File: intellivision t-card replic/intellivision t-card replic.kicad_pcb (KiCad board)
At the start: 2 copper layers, 143 x 165.9 mm, 77 parts, among them J1 2x22 card edge connector, SW1 SW_DIP_x08, SW2 SW_DIP_x08, SW3 SW_DIP_x08, SW4 SW_DIP_x08, U1 74LS374, U10 74LS00, U11 74LS85, U12 74LS51, U13 74LS00, U14 74LS85, U15 74LS51, U16 74LS00, U17 74LS85, U18 2732, U19 2732, U2 74LS374, U20 2732, U21 2732, U22 2732, U23 2732, U24 2732, U25 2732, U3 74LS42, U4 74LS04, U5 74LS08, U6 74LS51, U7 74LS00, U8 74LS85, U9 74LS51

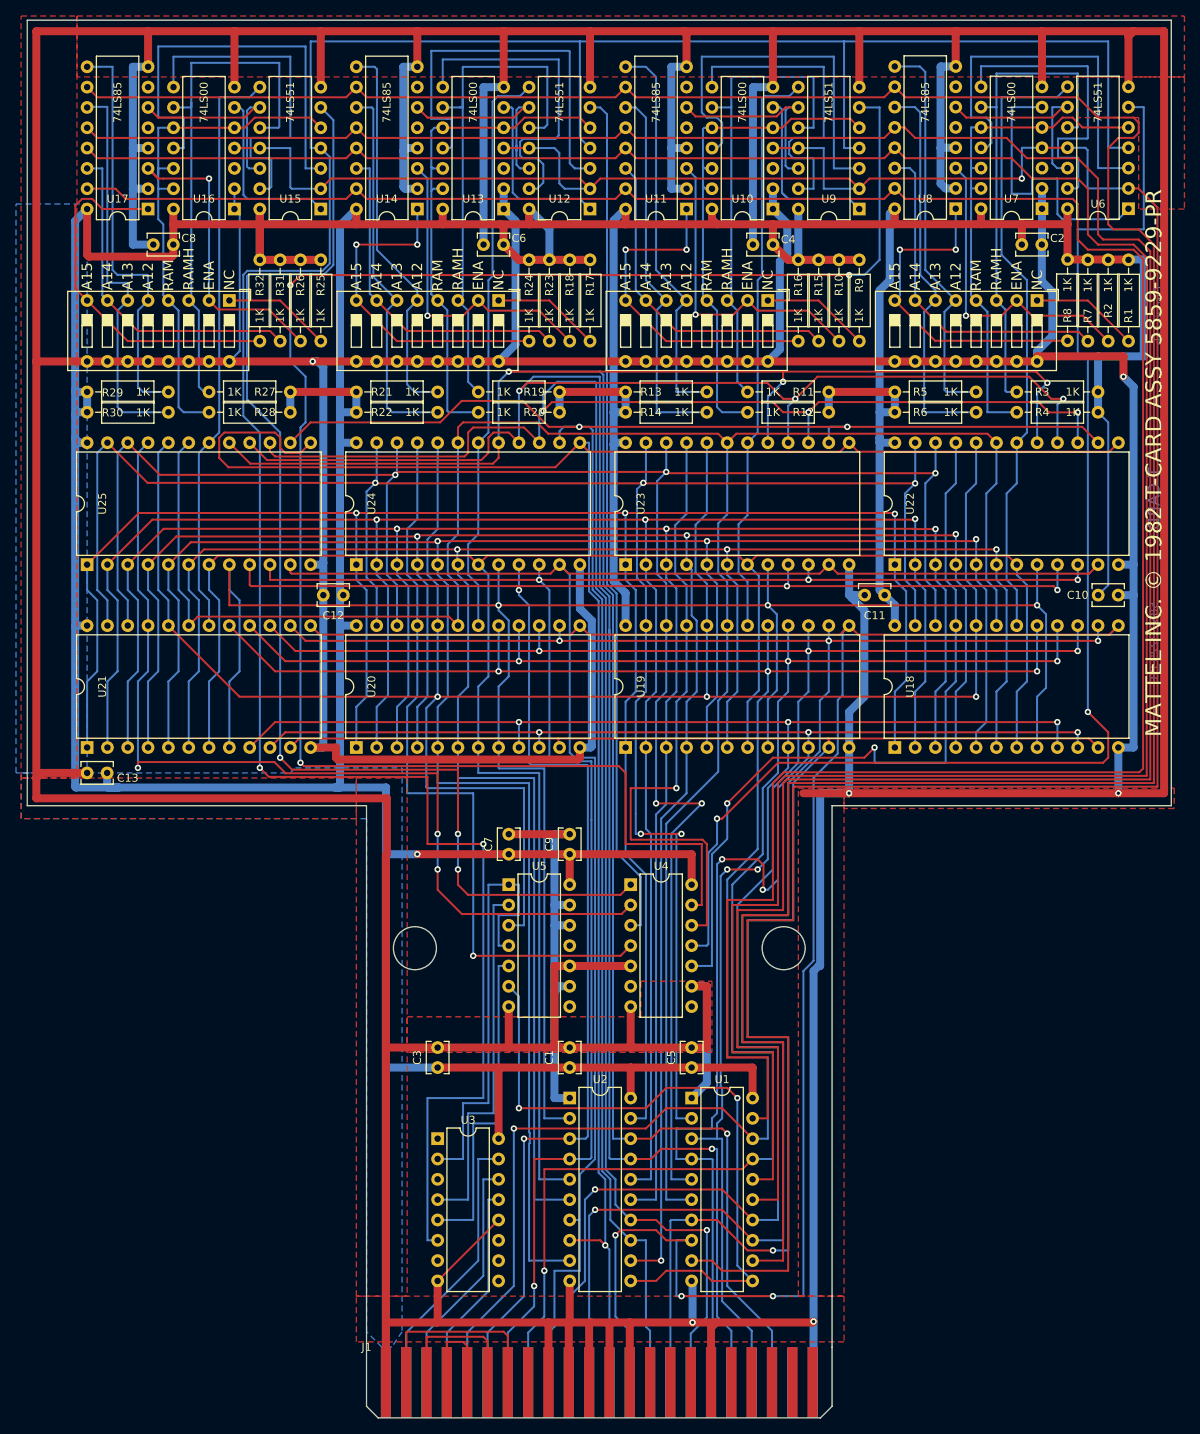
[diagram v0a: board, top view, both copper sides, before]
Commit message: added gitignore
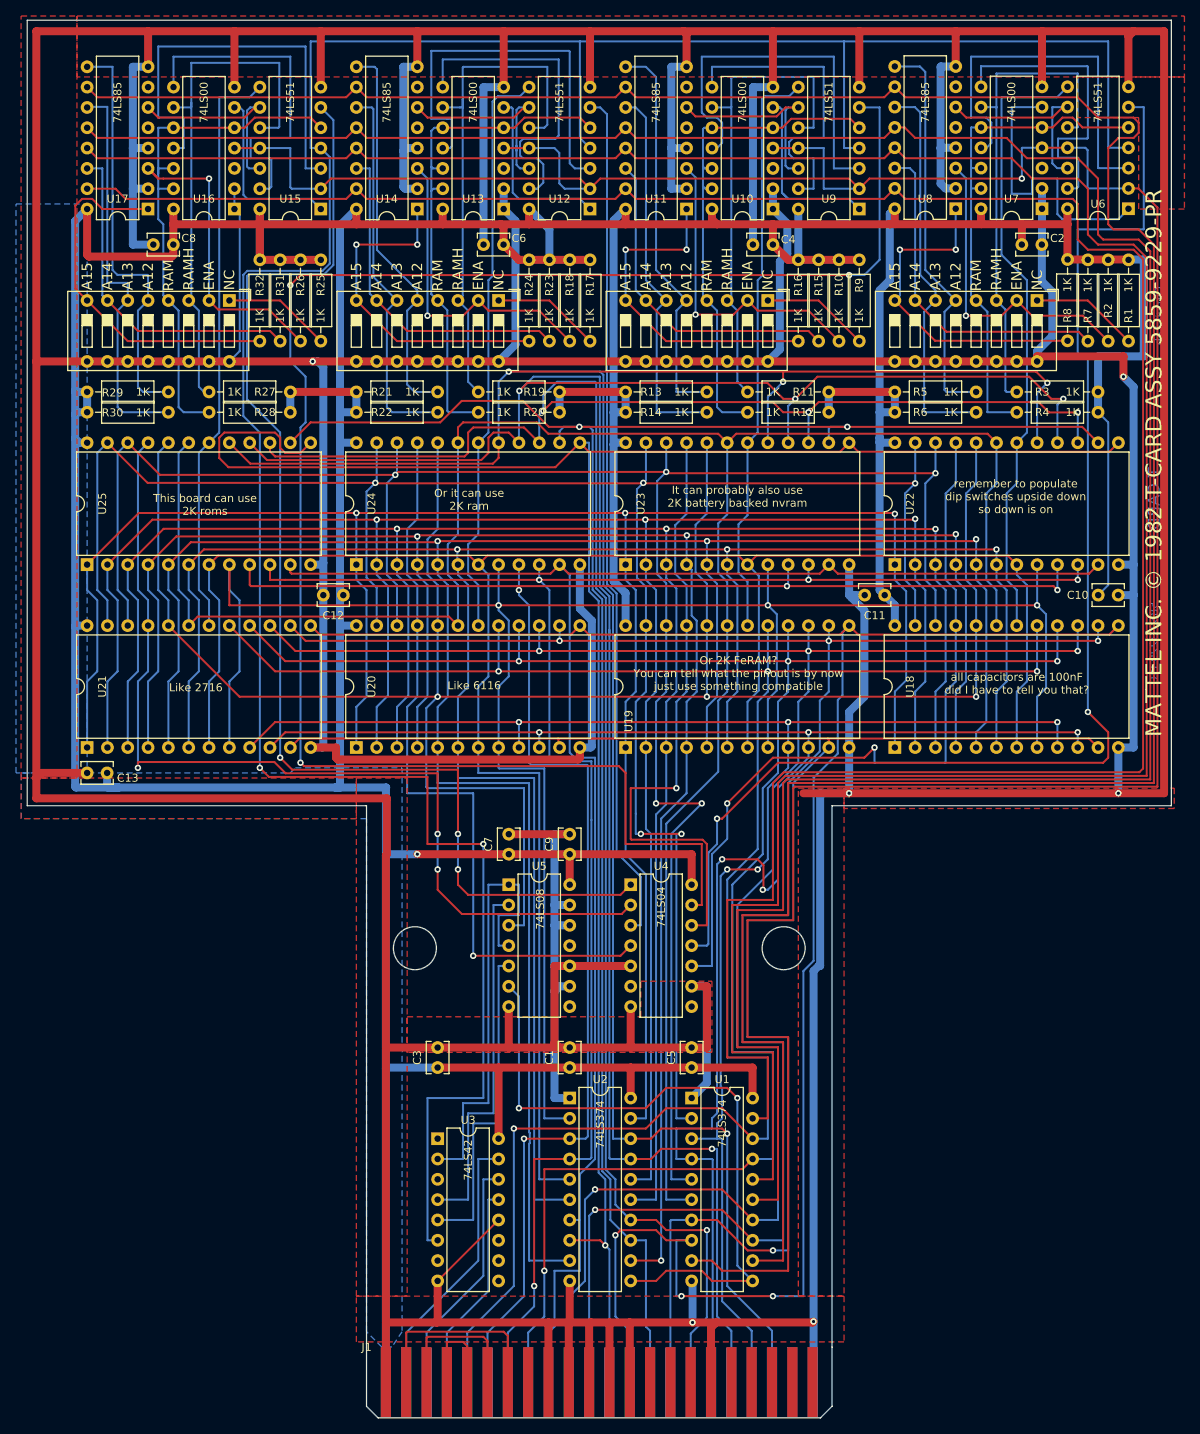
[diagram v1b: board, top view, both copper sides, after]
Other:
- board text added: "It can probably also use 2K battery backed nvram"
- board text added: "Like 2716"
- board text added: "Like 6116"
- board text added: "Or 2K FeRAM? You can tell what the pinout is by now just use something compatible"
- board text added: "Or it can use 2K ram"
- board text added: "This board can use 2K roms"
- board text added: "all capacitors are 100nF did I have to tell you that?"
- board text added: "remember to populate dip switches upside down so down is on"
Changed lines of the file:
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@@
       (effects (font (size 1 1) (thickness 0.15)))
     )
-    (fp_text value "74LS04" (at 3.81 17.57) (layer "F.Fab")
+    (fp_text value "74LS04" (at 3.81 2.794 90) (layer "F.SilkS")
       (effects (font (size 1 1) (thickness 0.15)))
     )
@@
       (effects (font (size 1 1) (thickness 0.15)))
     )
-    (fp_text value "74LS42" (at 3.81 20.11) (layer "F.Fab")
+    (fp_text value "74LS42" (at 3.81 2.667 90) (layer "F.SilkS")
       (effects (font (size 1 1) (thickness 0.15)))
     )
@@
       (effects (font (size 1 1) (thickness 0.15)))
     )
-    (fp_text value "74LS374" (at 3.81 25.19) (layer "F.Fab")
+    (fp_text value "74LS374" (at 3.81 3.302 90) (layer "F.SilkS")
       (effects (font (size 1 1) (thickness 0.15)))
     )
@@
       (effects (font (size 1 1) (thickness 0.15)))
     )
-    (fp_text value "74LS374" (at 3.81 25.19) (layer "F.Fab")
+    (fp_text value "74LS374" (at 3.81 3.175 90) (layer "F.SilkS")
       (effects (font (size 1 1) (thickness 0.15)))
     )
@@
     (property "Sheetname" "intellivision roms")
     (attr through_hole)
-    (fp_text reference "U19" (at 7.62 1.905 90) (layer "F.SilkS")
+    (fp_text reference "U19" (at 3.302 0.381 90) (layer "F.SilkS")
       (effects (font (size 1 1) (thickness 0.15)))
     )
@@
       (effects (font (size 1 1) (thickness 0.15)))
     )
-    (fp_text value "74LS08" (at 3.81 17.57) (layer "F.Fab")
+    (fp_text value "74LS08" (at 3.937 3.048 90) (layer "F.SilkS")
       (effects (font (size 1 1) (thickness 0.15)))
     )
@@
     (effects (font (size 1 1) (thickness 0.15)) (justify mirror))
   )
+  (gr_text "Like 6116" (at 102.362 100.838) (layer "F.SilkS")
+    (effects (font (size 1 1) (thickness 0.15)))
+  )
   (gr_text "A12" (at 128.905 51.435 90) (layer "F.SilkS")
     (effects (font (size 1.3 1.3) (thickness 0.2)) (justify left))
@@
     (effects (font (size 1.3 1.3) (thickness 0.2)) (justify left))
   )
+  (gr_text "Like 2716" (at 67.564 101.092) (layer "F.SilkS")
+    (effects (font (size 1 1) (thickness 0.15)))
+  )
   (gr_text "NC" (at 105.41 51.435 90) (layer "F.SilkS")
     (effects (font (size 1.3 1.3) (thickness 0.2)) (justify left))
@@
     (effects (font (size 1.3 1.3) (thickness 0.2)) (justify left))
   )
+  (gr_text "Or it can use \n2K ram" (at 101.727 77.597) (layer "F.SilkS")
+    (effects (font (size 1 1) (thickness 0.15)))
+  )
   (gr_text "RAMH" (at 66.675 51.435 90) (layer "F.SilkS")
     (effects (font (size 1.3 1.3) (thickness 0.2)) (justify left))
   )
+  (gr_text "remember to populate \ndip switches upside down\nso down is on" (at 170.053 77.216) (layer "F.SilkS")
+    (effects (font (size 1 1) (thickness 0.15)))
+  )
+  (gr_text "all capacitors are 100nF\ndid I have to tell you that?" (at 170.18 100.584) (layer "F.SilkS")
+    (effects (font (size 1 1) (thickness 0.15)))
+  )
   (gr_text "A12" (at 162.56 51.435 90) (layer "F.SilkS")
     (effects (font (size 1.3 1.3) (thickness 0.2)) (justify left))
@@
     (effects (font (size 1.3 1.3) (thickness 0.2)) (justify left))
   )
+  (gr_text "Or 2K FeRAM? \nYou can tell what the pinout is by now\njust use something compatible" (at 135.382 99.314) (layer "F.SilkS")
+    (effects (font (size 1 1) (thickness 0.15)))
+  )
   (gr_text "ENA" (at 102.87 51.435 90) (layer "F.SilkS")
     (effects (font (size 1.3 1.3) (thickness 0.2)) (justify left))
@@
     (effects (font (size 1.3 1.3) (thickness 0.2)) (justify left))
   )
+  (gr_text "It can probably also use \n2K battery backed nvram" (at 135.255 77.216) (layer "F.SilkS")
+    (effects (font (size 1 1) (thickness 0.15)))
+  )
   (gr_text "A13" (at 126.365 51.435 90) (layer "F.SilkS")
     (effects (font (size 1.3 1.3) (thickness 0.2)) (justify left))
@@
     (effects (font (size 1.3 1.3) (thickness 0.2)) (justify left))
   )
+  (gr_text "This board can use\n2K roms" (at 68.707 78.232) (layer "F.SilkS")
+    (effects (font (size 1 1) (thickness 0.15)))
+  )
   (gr_text "RAM" (at 165.1 51.565 90) (layer "F.SilkS")

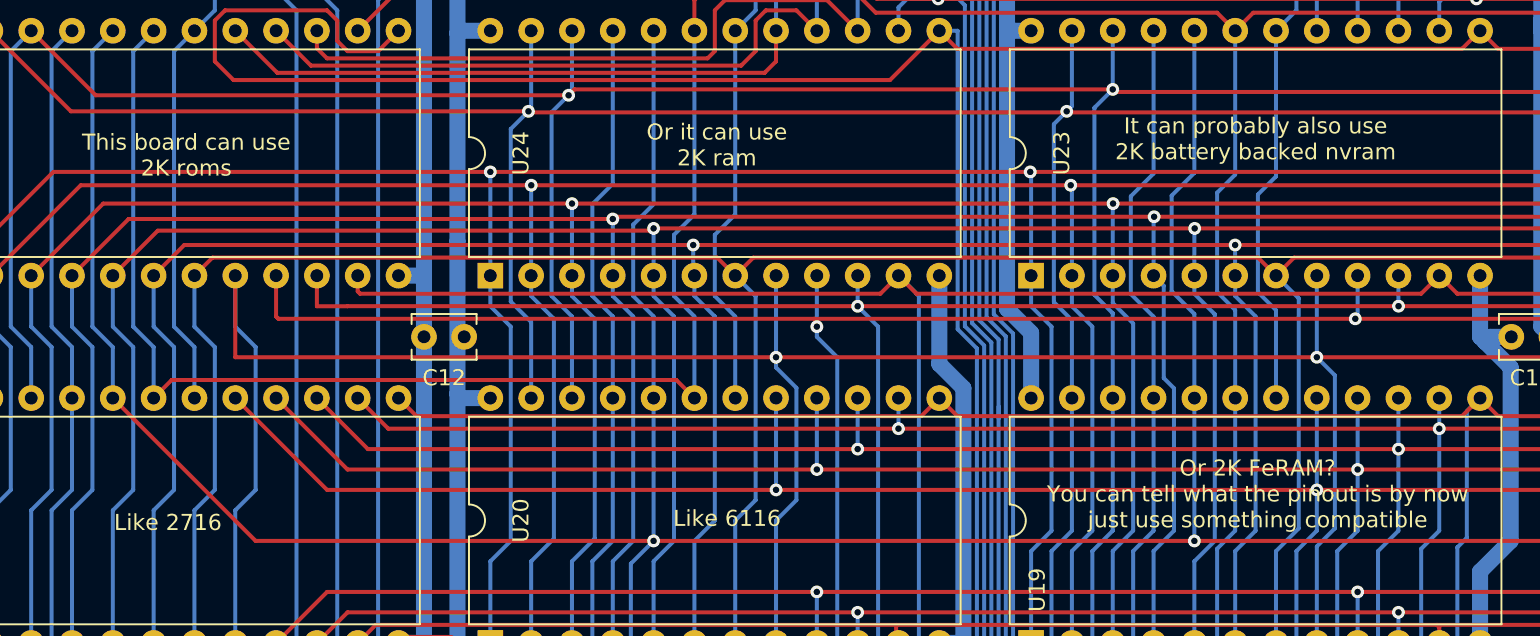
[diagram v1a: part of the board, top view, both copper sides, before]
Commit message: fixed silk about 2k/4k roms
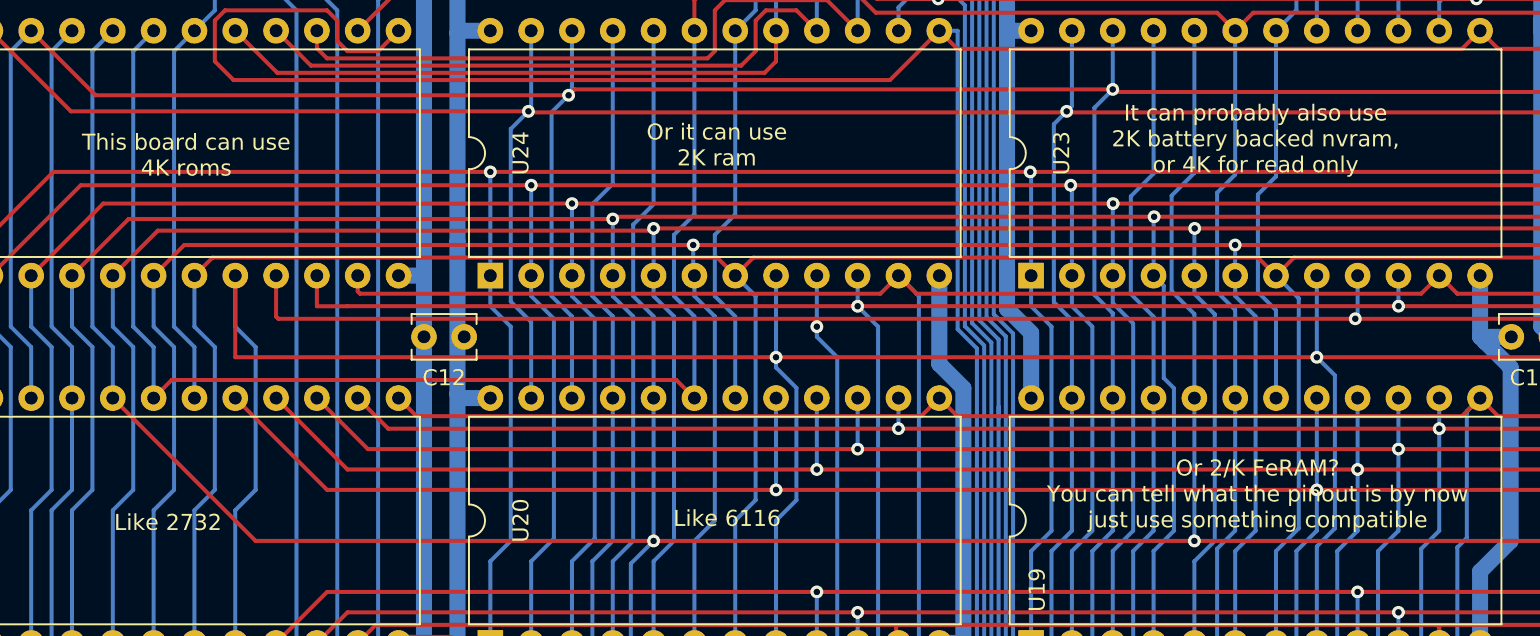
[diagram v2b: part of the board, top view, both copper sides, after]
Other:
- board text added: "It can probably also use 2K battery backed nvram, or 4K for read only"
- board text added: "Like 2732"
- board text added: "Or 2/K FeRAM? You can tell what the pinout is by now just use something compatible"
- board text added: "This board can use 4K roms"
- board text removed: "It can probably also use 2K battery backed nvram"
- board text removed: "Like 2716"
- board text removed: "Or 2K FeRAM? You can tell what the pinout is by now just use something compatible"
- board text removed: "This board can use 2K roms"
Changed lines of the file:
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@@
     (effects (font (size 1.3 1.3) (thickness 0.2)) (justify left))
   )
-  (gr_text "Like 2716" (at 67.564 101.092) (layer "F.SilkS")
+  (gr_text "Like 2732" (at 67.564 101.092) (layer "F.SilkS")
     (effects (font (size 1 1) (thickness 0.15)))
   )
@@
     (effects (font (size 1.3 1.3) (thickness 0.2)) (justify left))
   )
-  (gr_text "Or 2K FeRAM? \nYou can tell what the pinout is by now\njust use something compatible" (at 135.382 99.314) (layer "F.SilkS")
+  (gr_text "Or 2/K FeRAM? \nYou can tell what the pinout is by now\njust use something compatible" (at 135.382 99.314) (layer "F.SilkS")
     (effects (font (size 1 1) (thickness 0.15)))
   )
@@
     (effects (font (size 1.3 1.3) (thickness 0.2)) (justify left))
   )
-  (gr_text "It can probably also use \n2K battery backed nvram" (at 135.255 77.216) (layer "F.SilkS")
+  (gr_text "It can probably also use \n2K battery backed nvram, \nor 4K for read only" (at 135.255 77.216) (layer "F.SilkS")
     (effects (font (size 1 1) (thickness 0.15)))
   )
@@
     (effects (font (size 1.3 1.3) (thickness 0.2)) (justify left))
   )
-  (gr_text "This board can use\n2K roms" (at 68.707 78.232) (layer "F.SilkS")
+  (gr_text "This board can use\n4K roms" (at 68.707 78.232) (layer "F.SilkS")
     (effects (font (size 1 1) (thickness 0.15)))
   )
